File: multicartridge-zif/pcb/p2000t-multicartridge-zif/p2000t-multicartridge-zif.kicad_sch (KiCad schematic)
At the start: 15 parts, among them J1 P2000T_cartridge_edge, SW1 Soft Reset, SW2 SW_DIP_x05, U1 SST39SF040, U2 74HC123, U3 74HC00

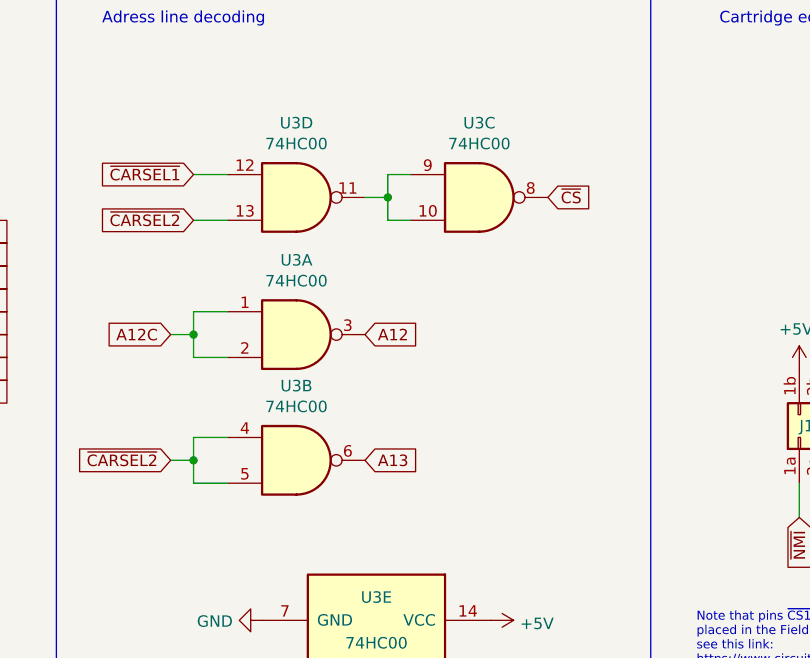
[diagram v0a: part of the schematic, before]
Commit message: Revision of ZIF cartridge
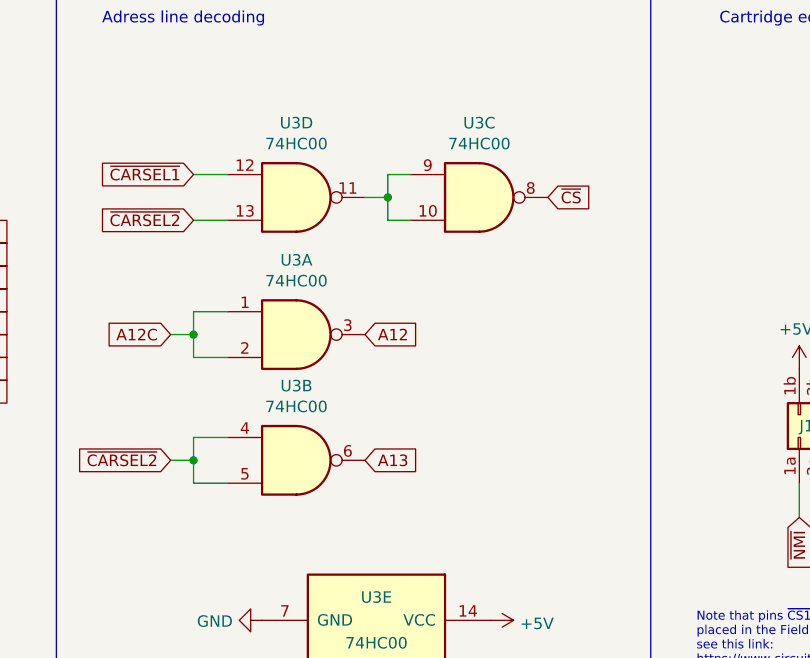
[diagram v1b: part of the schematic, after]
